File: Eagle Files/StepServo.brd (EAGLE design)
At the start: 43.6 x 43.2 mm, 8 parts, among them J2 1X2-3.5MM

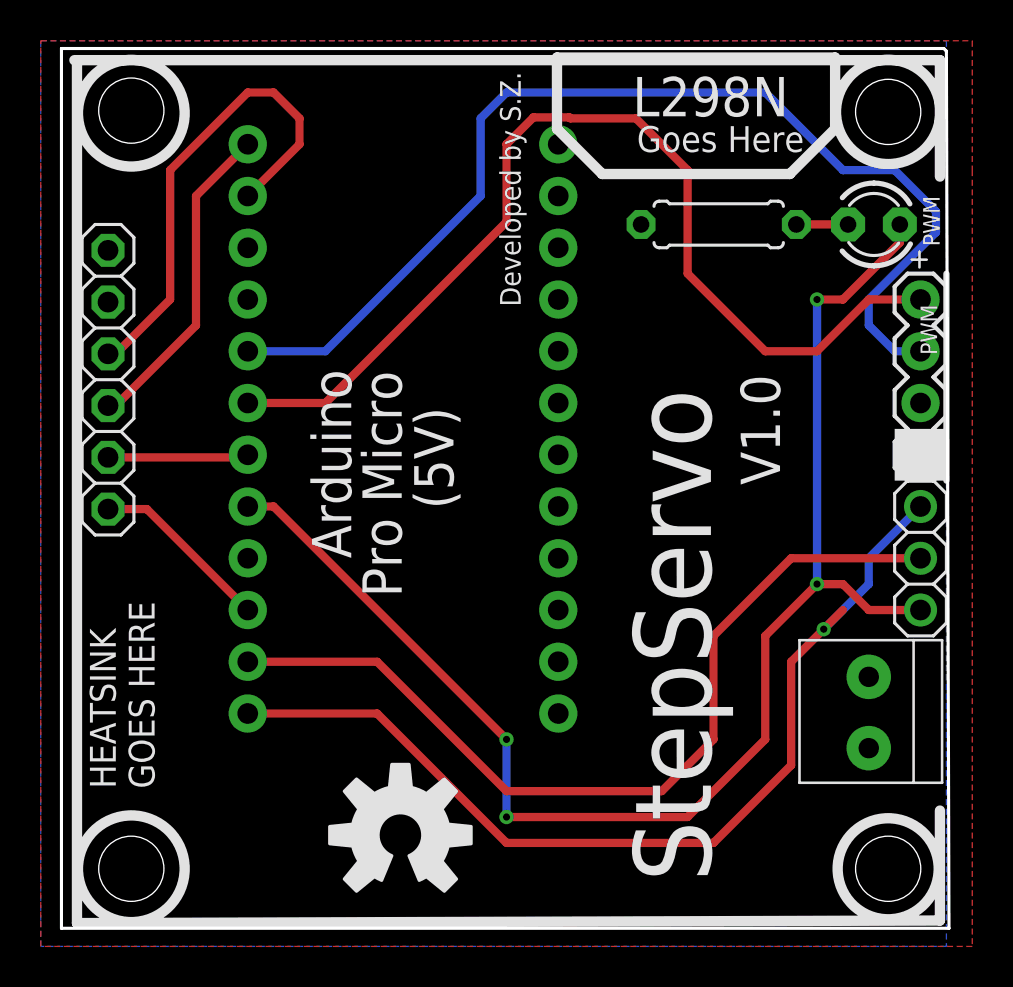
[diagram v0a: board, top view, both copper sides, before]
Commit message: Fixed some bad markers on silkscreen, and cleaned up schematic
Fixed some bad markers on silkscreen, and cleaned up schematic
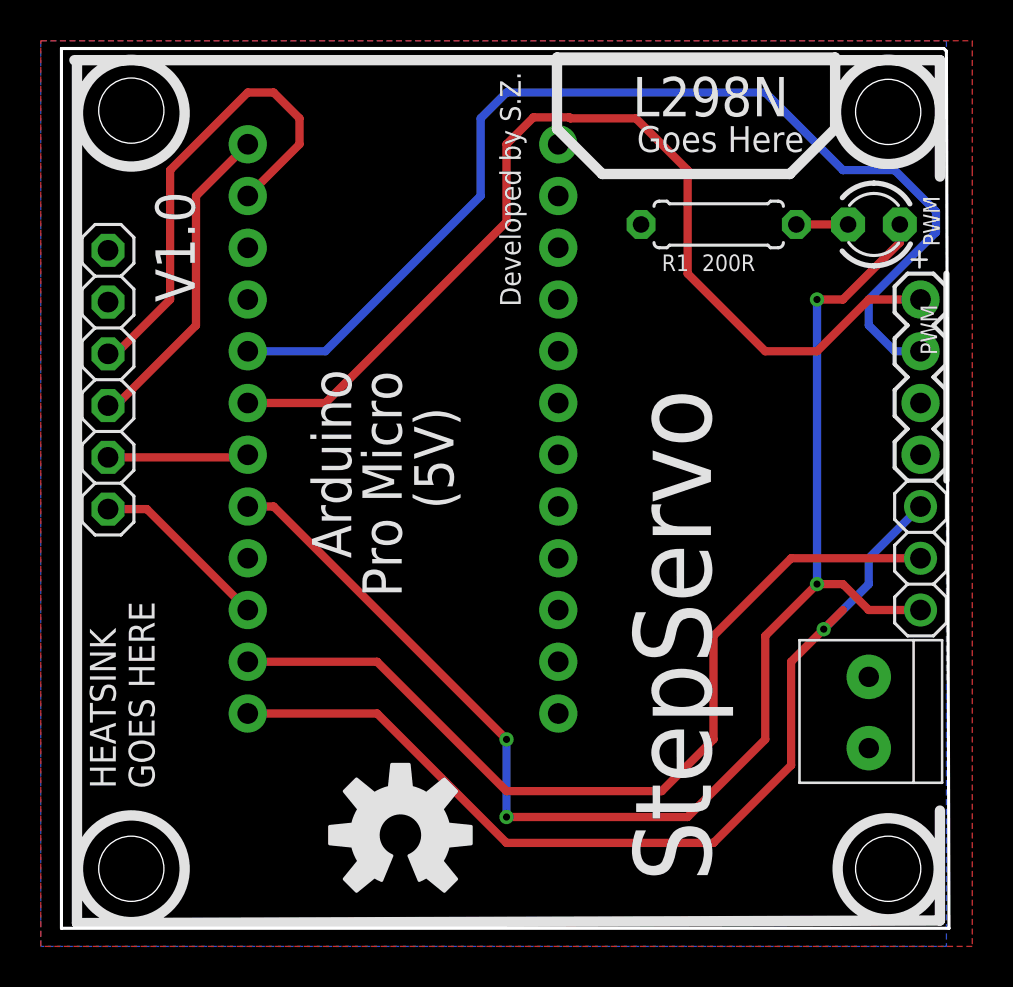
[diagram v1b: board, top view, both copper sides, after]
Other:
- board text added: "R1 200R"
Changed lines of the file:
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@@
 <hole x="55.5625" y="67.6275" drill="3.2"/>
 <wire x1="58.42" y1="59.69" x2="58.42" y2="49.53" width="0.3048" layer="21"/>
-<rectangle x1="55.88" y1="49.53" x2="58.42" y2="52.07" layer="21" rot="R180"/>
 <text x="29.21" y="45.72" size="1.9304" layer="21" font="vector" rot="R90">Arduino</text>
 <text x="50.673" y="69.342" size="1.9304" layer="21" font="vector" rot="R180">L298N</text>
@@
 <wire x1="51.562" y1="41.91" x2="49.53" y2="41.91" width="0.4064" layer="22"/>
 <wire x1="51.562" y1="59.436" x2="51.562" y2="41.91" width="0.4064" layer="22"/>
-<text x="48.3235" y="54.737" size="1.9304" layer="21" font="vector" rot="R270">V1.0</text>
+<text x="21.5265" y="58.293" size="1.9304" layer="21" font="vector" rot="R90">V1.0</text>
 <text x="27.559" y="68.199" size="1.27" layer="22" font="vector" rot="MR270">http://reprap.org/wiki/StepServo</text>
 <text x="57.277" y="63.5" size="0.8128" layer="21" font="vector" rot="R270">PWM</text>
+<text x="44.45" y="59.817" size="0.8128" layer="21" font="vector">R1  200R</text>
 </plain>
 <attributes>
